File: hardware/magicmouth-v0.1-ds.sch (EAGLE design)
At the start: 27 parts, among them IC1 LM386N, IC2 ATMEGA168-20P, J1 1X2-3.5MM, Q1 16Mhz, U1 ARDUINOR3-NOIOREF-NOTEXT, X1 STEREOJACK

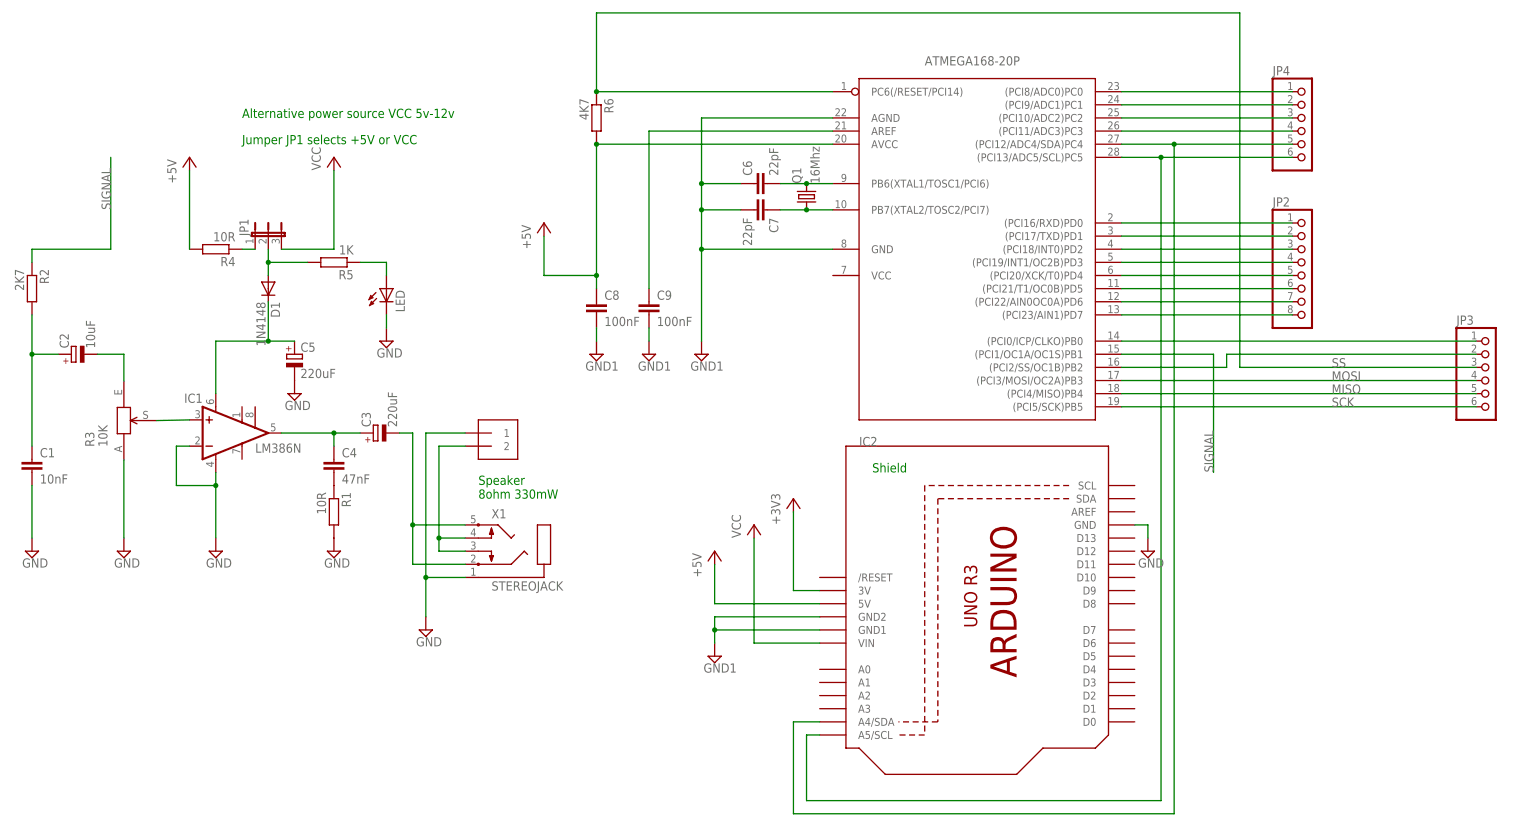
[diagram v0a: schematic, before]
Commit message: added programming jumpers
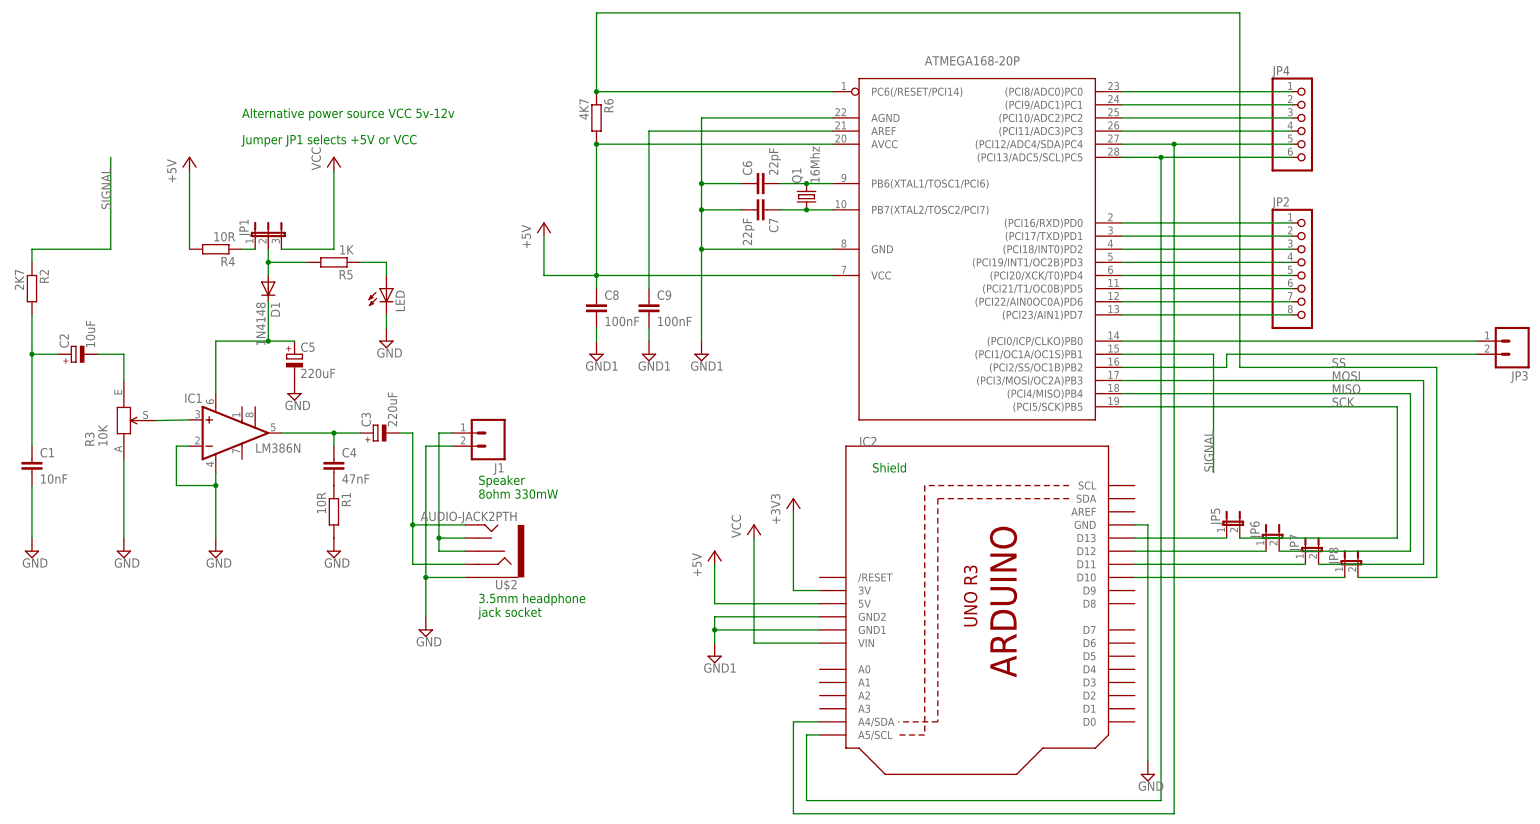
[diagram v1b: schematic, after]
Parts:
- removed X1: STEREOJACK, adafruit:STEREOJACK
- added JP5, JP6, JP7, JP8: (no value), SparkFun-Passives:JUMPER-2PTH
- added U$2: AUDIO-JACK2PTH, SparkFun-Connectors:AUDIO-JACK2PTH
- J1: value 1X2-3.5MM -> (none); device adafruit:1X2-3.5MM -> SparkFun-Connectors:M023.5MM
- JP3: device adafruit:PINHD-1X6B -> SparkFun-Connectors:M021X02_NO_SILK
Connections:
- new net N$90: JP5.1, U1.D13
- new net N$91: JP6.1, U1.D12
- new net N$92: JP7.1, U1.D11
- new net N$93: JP8.1, U1.D10
- net +5V: now also IC2.VCC
- net GND: now also J1.2, U$2.SLEEVE; no longer J1.1, X1.1
- net MISO: now also JP6.2; no longer JP3.5
- net MOSI: now also JP7.2; no longer JP3.4
- net N$3: now also J1.1, U$2.RSH, U$2.TSH; no longer J1.2, X1.3, X1.4
- net N$8: now also U$2.RING, U$2.TIP; no longer X1.2, X1.5
- net SCK: now also JP5.2; no longer JP3.6
- net SS: now also JP8.2; no longer JP3.3
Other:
- note added: "3.5mm headphone jack socket"
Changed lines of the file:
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@@
 <part name="GND13" library="supply2" deviceset="GND1" device=""/>
 <part name="JP2" library="adafruit" deviceset="PINHD-1X8" device="BIG"/>
-<part name="JP3" library="adafruit" deviceset="PINHD-1X6" device="B"/>
 <part name="P+1" library="supply1" deviceset="VCC" device=""/>
 <part name="P+2" library="supply1" deviceset="VCC" device=""/>
 <part name="GND14" library="supply2" deviceset="GND" device=""/>
 <part name="JP4" library="adafruit" deviceset="PINHD-1X6" device="B"/>
-<part name="X1" library="adafruit" deviceset="STEREOJACK" device=""/>
-<part name="J1" library="adafruit" deviceset="1X2" device="-3.5MM"/>
+<part name="J1" library="SparkFun-Connectors" deviceset="M02" device="3.5MM"/>
 <part name="P+5" library="supply1" deviceset="+5V" device=""/>
 <part name="P+6" library="supply1" deviceset="+5V" device=""/>
@@
 <part name="+3V1" library="supply1" deviceset="+3V3" device=""/>
 <part name="R3" library="t0mpr1c3" deviceset="TPOT" device="" technology="3352" value="10K"/>
+<part name="JP3" library="SparkFun-Connectors" deviceset="M02" device="1X02_NO_SILK"/>
+<part name="JP5" library="SparkFun-Passives" deviceset="JUMPER-2" device="PTH"/>
+<part name="JP6" library="SparkFun-Passives" deviceset="JUMPER-2" device="PTH"/>
+<part name="JP7" library="SparkFun-Passives" deviceset="JUMPER-2" device="PTH"/>
+<part name="JP8" library="SparkFun-Passives" deviceset="JUMPER-2" device="PTH"/>
+<part name="U$2" library="SparkFun-Connectors" deviceset="AUDIO-JACK2" device="PTH"/>
 </parts>
 <sheets>
@@
 <text x="63.5" y="124.46" size="1.778" layer="91">Alternative power source VCC 5v-12v</text>
 <text x="185.42" y="55.88" size="1.778" layer="91">Shield</text>
+<text x="109.22" y="27.94" size="1.778" layer="91">3.5mm headphone
+jack socket</text>
 </plain>
 <instances>
@@
 <instance part="GND13" gate="G$1" x="154.94" y="20.32"/>
 <instance part="JP2" gate="G$1" x="269.24" y="96.52"/>
-<instance part="JP3" gate="A" x="304.8" y="73.66"/>
 <instance part="P+1" gate="VCC" x="162.56" y="45.72"/>
 <instance part="P+2" gate="VCC" x="81.28" y="116.84"/>
-<instance part="GND14" gate="GND" x="238.76" y="40.64"/>
+<instance part="GND14" gate="GND" x="238.76" y="-2.54"/>
 <instance part="JP4" gate="A" x="269.24" y="121.92"/>
-<instance part="X1" gate="1" x="119.38" y="43.18"/>
-<instance part="J1" gate="G$1" x="111.76" y="60.96"/>
+<instance part="J1" gate="G$1" x="111.76" y="63.5" rot="R180"/>
 <instance part="P+5" gate="1" x="154.94" y="40.64"/>
 <instance part="P+6" gate="1" x="121.92" y="104.14"/>
@@
 <instance part="+3V1" gate="G$1" x="170.18" y="50.8"/>
 <instance part="R3" gate="G$1" x="40.64" y="66.04"/>
+<instance part="JP3" gate="G$1" x="309.88" y="81.28" rot="R180"/>
+<instance part="JP5" gate="A" x="254" y="45.72"/>
+<instance part="JP6" gate="A" x="261.62" y="43.18"/>
+<instance part="JP7" gate="A" x="269.24" y="40.64"/>
+<instance part="JP8" gate="A" x="276.86" y="38.1"/>
+<instance part="U$2" gate="G$1" x="111.76" y="40.64" rot="R180"/>
 </instances>
 <busses>
@@
 </segment>
 <segment>
-<wire x1="99.06" y1="63.5" x2="99.06" y2="35.56" width="0.1524" layer="91"/>
 <pinref part="GND6" gate="GND" pin="GND"/>
-<pinref part="X1" gate="1" pin="1"/>
 <wire x1="99.06" y1="35.56" x2="99.06" y2="27.94" width="0.1524" layer="91"/>
 <wire x1="106.68" y1="35.56" x2="99.06" y2="35.56" width="0.1524" layer="91"/>
+<pinref part="J1" gate="G$1" pin="2"/>
+<wire x1="104.14" y1="60.96" x2="99.06" y2="60.96" width="0.1524" layer="91"/>
+<wire x1="99.06" y1="60.96" x2="99.06" y2="35.56" width="0.1524" layer="91"/>
 <junction x="99.06" y="35.56"/>
-<pinref part="J1" gate="G$1" pin="1"/>
-<wire x1="106.68" y1="63.5" x2="99.06" y2="63.5" width="0.1524" layer="91"/>
+<pinref part="U$2" gate="G$1" pin="SLEEVE"/>
 </segment>
 <segment>
@@
 <pinref part="GND14" gate="GND" pin="GND"/>
 <wire x1="236.22" y1="45.72" x2="238.76" y2="45.72" width="0.1524" layer="91"/>
-<wire x1="238.76" y1="45.72" x2="238.76" y2="43.18" width="0.1524" layer="91"/>
+<wire x1="238.76" y1="45.72" x2="238.76" y2="0" width="0.1524" layer="91"/>
 </segment>
 <segment>
@@
 <junction x="132.08" y="129.54"/>
 <wire x1="256.54" y1="144.78" x2="256.54" y2="76.2" width="0.1524" layer="91"/>
-<pinref part="JP3" gate="A" pin="3"/>
-<wire x1="256.54" y1="76.2" x2="302.26" y2="76.2" width="0.1524" layer="91"/>
+<wire x1="256.54" y1="76.2" x2="294.64" y2="76.2" width="0.1524" layer="91"/>
 <label x="274.32" y="76.2" size="1.778" layer="95"/>
+<pinref part="JP8" gate="A" pin="2"/>
+<wire x1="279.4" y1="35.56" x2="294.64" y2="35.56" width="0.1524" layer="91"/>
+<wire x1="294.64" y1="76.2" x2="294.64" y2="35.56" width="0.1524" layer="91"/>
 </segment>
 </net>
@@
 <segment>
 <pinref part="IC2" gate="G$1" pin="(PCI0/ICP/CLKO)PB0"/>
-<pinref part="JP3" gate="A" pin="1"/>
 <wire x1="233.68" y1="81.28" x2="302.26" y2="81.28" width="0.1524" layer="91"/>
+<pinref part="JP3" gate="G$1" pin="1"/>
 </segment>
 </net>
@@
 <segment>
 <pinref part="IC2" gate="G$1" pin="(PCI4/MISO)PB4"/>
-<pinref part="JP3" gate="A" pin="5"/>
-<wire x1="233.68" y1="71.12" x2="302.26" y2="71.12" width="0.1524" layer="91"/>
+<wire x1="233.68" y1="71.12" x2="289.56" y2="71.12" width="0.1524" layer="91"/>
 <label x="274.32" y="71.12" size="1.778" layer="95"/>
+<pinref part="JP6" gate="A" pin="2"/>
+<wire x1="264.16" y1="40.64" x2="289.56" y2="40.64" width="0.1524" layer="91"/>
+<wire x1="289.56" y1="40.64" x2="289.56" y2="71.12" width="0.1524" layer="91"/>
 </segment>
 </net>
@@
 <segment>
 <pinref part="IC2" gate="G$1" pin="(PCI5/SCK)PB5"/>
-<pinref part="JP3" gate="A" pin="6"/>
-<wire x1="233.68" y1="68.58" x2="302.26" y2="68.58" width="0.1524" layer="91"/>
+<wire x1="233.68" y1="68.58" x2="287.02" y2="68.58" width="0.1524" layer="91"/>
 <label x="274.32" y="68.58" size="1.778" layer="95"/>
+<pinref part="JP5" gate="A" pin="2"/>
+<wire x1="256.54" y1="43.18" x2="287.02" y2="43.18" width="0.1524" layer="91"/>
+<wire x1="287.02" y1="43.18" x2="287.02" y2="68.58" width="0.1524" layer="91"/>
 </segment>
 </net>
@@
 <wire x1="132.08" y1="93.98" x2="121.92" y2="93.98" width="0.1524" layer="91"/>
 <wire x1="121.92" y1="93.98" x2="121.92" y2="101.6" width="0.1524" layer="91"/>
+<pinref part="IC2" gate="G$1" pin="VCC"/>
+<wire x1="177.8" y1="93.98" x2="132.08" y2="93.98" width="0.1524" layer="91"/>
 </segment>
 <segment>
@@
 <segment>
 <pinref part="IC2" gate="G$1" pin="(PCI3/MOSI/OC2A)PB3"/>
-<pinref part="JP3" gate="A" pin="4"/>
-<wire x1="233.68" y1="73.66" x2="302.26" y2="73.66" width="0.1524" layer="91"/>
+<wire x1="233.68" y1="73.66" x2="292.1" y2="73.66" width="0.1524" layer="91"/>
 <label x="274.32" y="73.66" size="1.778" layer="95"/>
+<pinref part="JP7" gate="A" pin="2"/>
+<wire x1="271.78" y1="38.1" x2="292.1" y2="38.1" width="0.1524" layer="91"/>
+<wire x1="292.1" y1="38.1" x2="292.1" y2="73.66" width="0.1524" layer="91"/>
 </segment>
 </net>
@@
 <net name="N$3" class="0">
 <segment>
-<pinref part="X1" gate="1" pin="3"/>
 <wire x1="106.68" y1="40.64" x2="101.6" y2="40.64" width="0.1524" layer="91"/>
 <wire x1="101.6" y1="40.64" x2="101.6" y2="43.18" width="0.1524" layer="91"/>
-<pinref part="X1" gate="1" pin="4"/>
 <wire x1="106.68" y1="43.18" x2="101.6" y2="43.18" width="0.1524" layer="91"/>
-<wire x1="101.6" y1="43.18" x2="101.6" y2="60.96" width="0.1524" layer="91"/>
-<pinref part="J1" gate="G$1" pin="2"/>
-<wire x1="101.6" y1="60.96" x2="106.68" y2="60.96" width="0.1524" layer="91"/>
+<wire x1="101.6" y1="43.18" x2="101.6" y2="63.5" width="0.1524" layer="91"/>
 <junction x="101.6" y="43.18"/>
+<pinref part="J1" gate="G$1" pin="1"/>
+<wire x1="101.6" y1="63.5" x2="104.14" y2="63.5" width="0.1524" layer="91"/>
+<pinref part="U$2" gate="G$1" pin="RSH"/>
+<pinref part="U$2" gate="G$1" pin="TSH"/>
 </segment>
 </net>
@@
 <wire x1="93.98" y1="63.5" x2="96.52" y2="63.5" width="0.1524" layer="91"/>
 <wire x1="96.52" y1="63.5" x2="96.52" y2="45.72" width="0.1524" layer="91"/>
-<pinref part="X1" gate="1" pin="5"/>
 <wire x1="96.52" y1="45.72" x2="106.68" y2="45.72" width="0.1524" layer="91"/>
-<pinref part="X1" gate="1" pin="2"/>
 <wire x1="106.68" y1="38.1" x2="96.52" y2="38.1" width="0.1524" layer="91"/>
 <wire x1="96.52" y1="38.1" x2="96.52" y2="45.72" width="0.1524" layer="91"/>
 <junction x="96.52" y="45.72"/>
+<pinref part="U$2" gate="G$1" pin="RING"/>
+<pinref part="U$2" gate="G$1" pin="TIP"/>
 </segment>
 </net>
@@
 <wire x1="233.68" y1="76.2" x2="254" y2="76.2" width="0.1524" layer="91"/>
 <wire x1="254" y1="76.2" x2="254" y2="78.74" width="0.1524" layer="91"/>
-<pinref part="JP3" gate="A" pin="2"/>
 <wire x1="254" y1="78.74" x2="302.26" y2="78.74" width="0.1524" layer="91"/>
-</segment>
-</net>
+<pinref part="JP3" gate="G$1" pin="2"/>
+</segment>
+</net>
+<net name="N$90" class="0">
+<segment>
+<pinref part="U1" gate="G$1" pin="D13"/>
+<pinref part="JP5" gate="A" pin="1"/>
+<wire x1="236.22" y1="43.18" x2="254" y2="43.18" width="0.1524" layer="91"/>
+</segment>
+</net>
+<net name="N$91" class="0">
+<segment>
+<pinref part="U1" gate="G$1" pin="D12"/>
+<pinref part="JP6" gate="A" pin="1"/>
+<wire x1="236.22" y1="40.64" x2="261.62" y2="40.64" width="0.1524" layer="91"/>
+</segment>
+</net>
+<net name="N$92" class="0">
+<segment>
+<pinref part="U1" gate="G$1" pin="D11"/>
+<pinref part="JP7" gate="A" pin="1"/>
+<wire x1="236.22" y1="38.1" x2="269.24" y2="38.1" width="0.1524" layer="91"/>
+</segment>
+</net>
+<net name="N$93" class="0">
+<segment>
+<pinref part="U1" gate="G$1" pin="D10"/>
+<pinref part="JP8" gate="A" pin="1"/>
+<wire x1="236.22" y1="35.56" x2="276.86" y2="35.56" width="0.1524" layer="91"/>
+</segment>
+</net>

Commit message: reset switch on ss board; optional capacitor
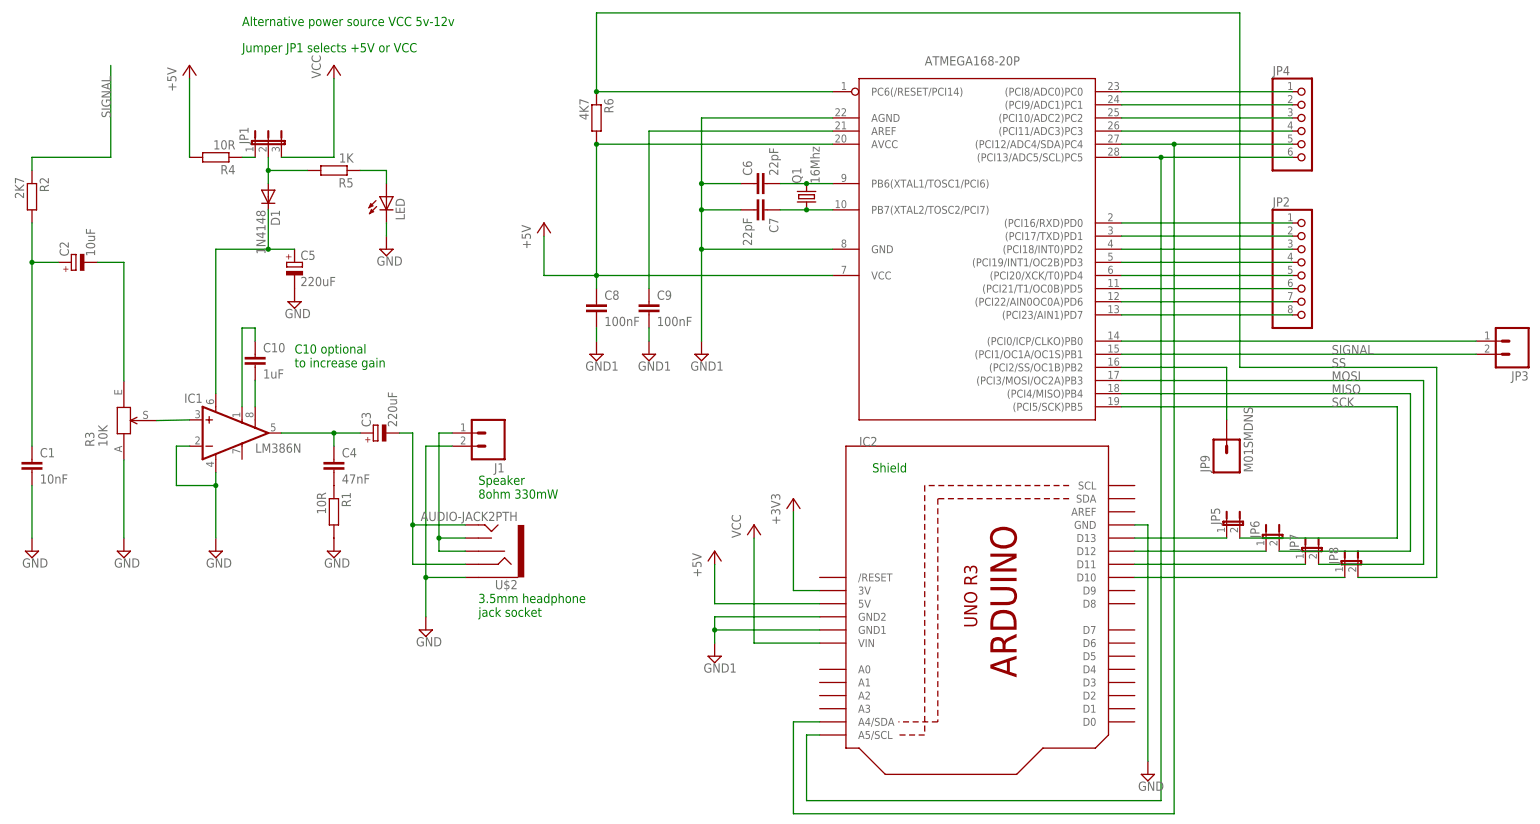
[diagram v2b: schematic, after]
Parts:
- added C10: 1uF, rcl:C-EU050-025X075
- added JP9: M01SMDNS, SparkFun-Connectors:M01SMDNS
- C1: device resistor:C-EU025-025X050 -> rcl:C-EU050-025X075
- C2: device resistor:CPOL-EUE2.5-6 -> rcl:CPOL-EUE2.5-7
- C4: device rcl:C-EU025-025X050 -> rcl:C-EU050-025X075
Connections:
- new net N$98: C10.1, IC1.GAIN@1
- new net N$99: C10.2, IC1.GAIN@2
- net N$12: now also JP9.1; no longer JP3.2
- net SIGNAL: now also JP3.2
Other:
- note added: "C10 optional to increase gain"
- moved on the sheet: C2, C5, D1, JP1, LED, R2, R4, R5
